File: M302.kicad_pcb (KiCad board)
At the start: 2 copper layers, 68.6 x 53.3 mm, 22 parts, among them J1 I2C-SHT3x, J2 I2C-ThmCp, J3 I2C-3, J4 I2C-4, J5 I2C-D400, J6 W5500, J7 IM920, J8 PWR, P1 Power, P2 Analog, P3 Digital, P4 Digital, P5 CONN_01X01, P6 CONN_01X01, P7 CONN_01X01, P8 CONN_01X01, SW1 CPU, SW2 D400, SW3 IM920, U1 SFE-BOB-12009

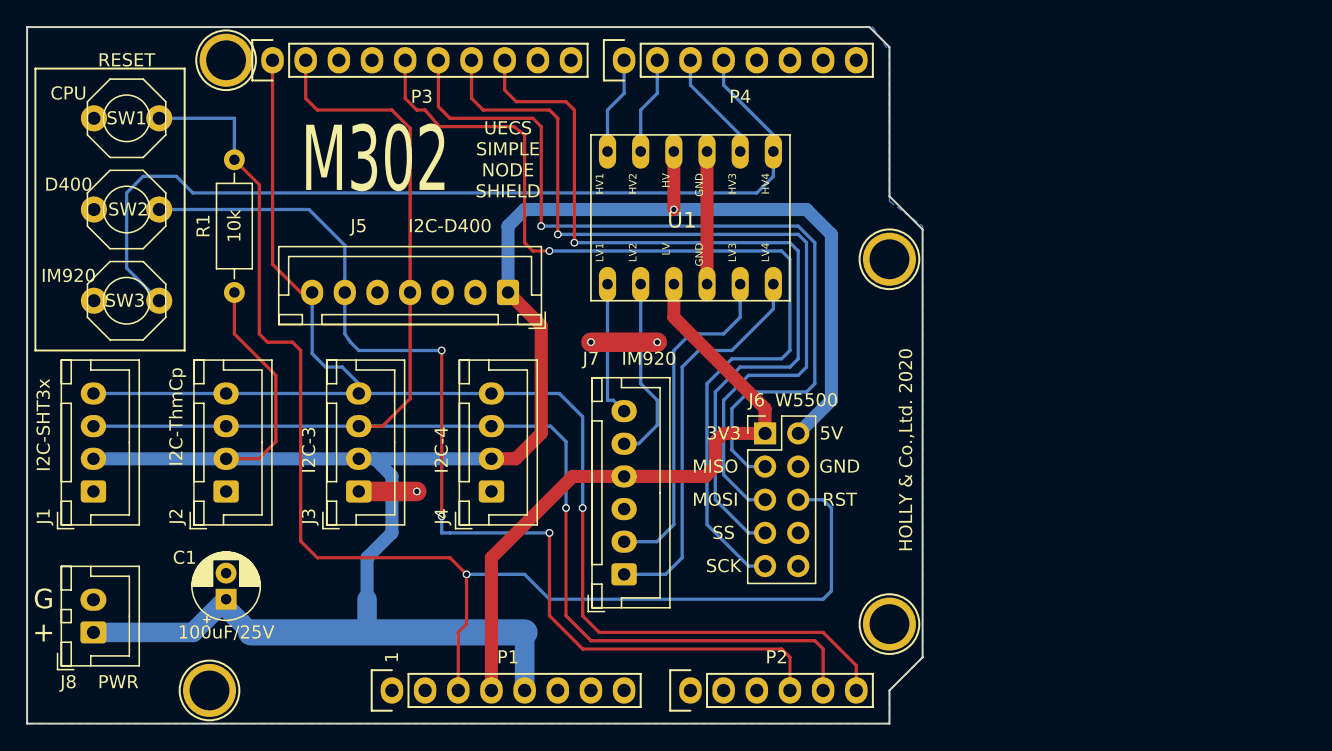
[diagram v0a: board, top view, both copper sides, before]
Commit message: sch: 1.10 PullUp抵抗とアナログインプットを増やす
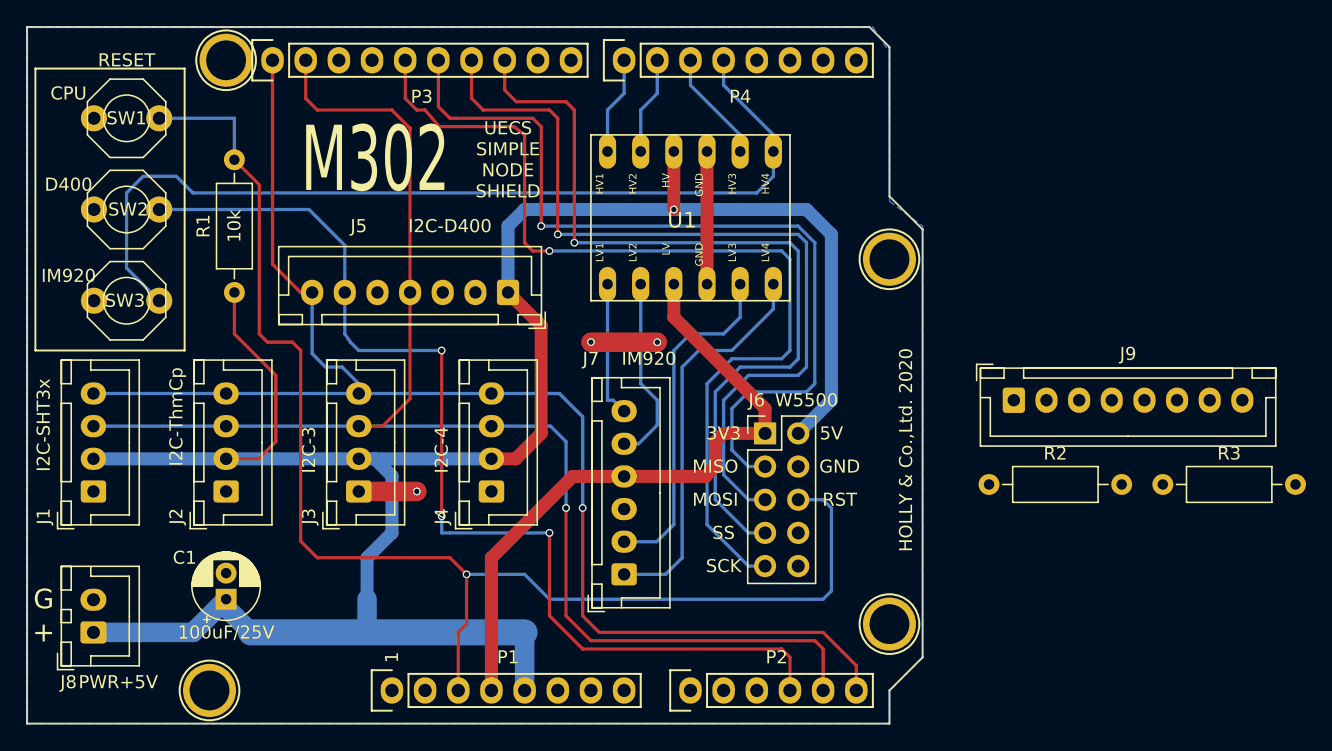
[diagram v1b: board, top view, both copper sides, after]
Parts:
- added J9: ANALOG-IN, Connector_JST:JST_XH_B8B-XH-A_1x08_P2.50mm_Vertical, F.Cu at (186.6, 101.6)
- added R2: 10k, Resistor_THT:R_Axial_DIN0207_L6.3mm_D2.5mm_P10.16mm_Horizontal, F.Cu at (184.7, 108.0)
- added R3: 10k, Resistor_THT:R_Axial_DIN0207_L6.3mm_D2.5mm_P10.16mm_Horizontal, F.Cu at (198.0, 108.0)
- J8: value PWR -> PWR+5V
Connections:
- J5 pad 6: /A3 -> /3(**)
- P2 pad 1: /A0 -> Net-(J9-Pad1)
- P2 pad 2: /A1 -> Net-(J9-Pad3)
- P2 pad 3: /A2 -> Net-(J9-Pad5)
- P2 pad 4: /A3 -> Net-(J9-Pad7)
- SW2 pad 2: /A3 -> /3(**)

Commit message: M302改 v1.10 PCB作業途中
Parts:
- R1, R2, R3: footprint Resistor_THT:R_Axial_DIN0207_L6.3mm_D2.5mm_P10.16mm_Horizontal -> Resistor_THT:R_Axial_DIN0207_L6.3mm_D2.5mm_P7.62mm_Horizontal
- moved R2 60.1 mm to (127.5, 89.5), turned to 90 degrees
- moved J9 40.7 mm to (149.1, 117.5), turned to 90 degrees
- moved R3 38.3 mm to (172.6, 79.4), turned to 270 degrees
- moved J4 5.72 mm to (140.8, 108.6)
- moved R1 4.45 mm to (124.6, 89.5)
- moved J3 3.81 mm to (132.6, 108.6)
- moved J2 1.91 mm to (124.3, 108.6)
- moved J7 1.27 mm to (158.0, 114.9)
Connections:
- P2 pad 5: /A4(SDA) -> Net-(P2-Pad5)
- P2 pad 6: /A5(SCL) -> Net-(P2-Pad6)
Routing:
- net /A3: track 81.0 -> 0.00 mm, vias 3 -> 0
- net /A5(SCL): track 107.4 -> 60.0 mm, vias 1 -> 0
- net /A4(SDA): track 111.3 -> 67.9 mm, vias 1 -> 0
- net +3V3: track 50.5 -> 14.3 mm
- net /3(**): track 0.00 -> 18.6 mm
- net +5V: track 171.7 -> 160.0 mm
- net /Reset: track 102.4 -> 90.8 mm
- net (no net): track 5.08 -> 0.00 mm, vias 2 -> 0
- net GND: track 14.6 -> 10.2 mm

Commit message: pcb: M302改 v1.10 PCB作業一旦終了
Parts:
- moved J9 1.27 mm to (150.4, 117.5)
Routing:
- net +3V3: track 14.3 -> 73.6 mm
- net /3(**): track 18.6 -> 67.5 mm, vias 0 -> 2
- net /Reset: track 90.8 -> 133.9 mm, vias 1 -> 2
- net Net-(J9-Pad7): track 0.00 -> 36.1 mm
- net Net-(J9-Pad5): track 0.00 -> 29.1 mm
- net Net-(J9-Pad3): track 0.00 -> 22.3 mm
- net +5V: track 160.0 -> 176.9 mm, vias 1 -> 2
- net Net-(J9-Pad1): track 0.00 -> 15.0 mm
- net GND: track 10.2 -> 24.1 mm, vias 1 -> 61
- net /A4(SDA): track 67.9 -> 58.4 mm, vias 0 -> 1
- net /4: track 70.9 -> 77.5 mm
- net /A5(SCL): track 60.0 -> 54.3 mm
- net Net-(J7-Pad2): track 26.4 -> 25.1 mm
- net Net-(J7-Pad1): track 30.3 -> 29.0 mm
- net /13(SCK): track 73.3 -> 74.4 mm
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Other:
- board text added: "HOLLY & Co.,Ltd. 2021"
- board text added: "K A I"
- board text removed: "HOLLY & Co.,Ltd. 2020"

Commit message: sche: board: docs:
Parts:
- added C2: 0.01μF, Capacitor_THT:C_Disc_D3.0mm_W2.0mm_P2.50mm, F.Cu at (138.3, 119.4)
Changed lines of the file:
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@@
-(kicad_pcb (version 20171130) (host pcbnew 5.1.5+dfsg1-2build2)
+(kicad_pcb (version 20171130) (host pcbnew 5.1.6-c6e7f7d~87~ubuntu18.04.1)
   (general
     (thickness 1.6)
@@
     (tracks 322)
     (zones 0)
-    (modules 25)
+    (modules 26)
     (nets 43)
   )
@@
     (add_net "Net-(P8-Pad1)")
   )
+  (module Capacitor_THT:C_Disc_D3.0mm_W2.0mm_P2.50mm (layer F.Cu)
+    (at 138.303 119.38 90)
+    (descr "C, Disc series, Radial, pin pitch=2.50mm, , diameter*width=3*2mm^2, Capacitor")
+    (tags "C Disc series Radial pin pitch 2.50mm  diameter 3mm width 2mm Capacitor")
+    (fp_text reference C2 (at 3.175 -2.54 180) (layer F.SilkS)
+      (effects (font (size 1 1) (thickness 0.15)))
+    )
+    (fp_text value 0.01μF (at 0.635 4.445 180) (layer F.SilkS)
+      (effects (font (size 1 1) (thickness 0.15)))
+    )
+    (fp_line (start 3.55 -1.25) (end -1.05 -1.25) (layer F.CrtYd) (width 0.05))
+    (fp_line (start 3.55 1.25) (end 3.55 -1.25) (layer F.CrtYd) (width 0.05))
+    (fp_line (start -1.05 1.25) (end 3.55 1.25) (layer F.CrtYd) (width 0.05))
+    (fp_line (start -1.05 -1.25) (end -1.05 1.25) (layer F.CrtYd) (width 0.05))
+    (fp_line (start 2.87 1.055) (end 2.87 1.12) (layer F.SilkS) (width 0.12))
+    (fp_line (start 2.87 -1.12) (end 2.87 -1.055) (layer F.SilkS) (width 0.12))
+    (fp_line (start -0.37 1.055) (end -0.37 1.12) (layer F.SilkS) (width 0.12))
+    (fp_line (start -0.37 -1.12) (end -0.37 -1.055) (layer F.SilkS) (width 0.12))
+    (fp_line (start -0.37 1.12) (end 2.87 1.12) (layer F.SilkS) (width 0.12))
+    (fp_line (start -0.37 -1.12) (end 2.87 -1.12) (layer F.SilkS) (width 0.12))
+    (fp_line (start 2.75 -1) (end -0.25 -1) (layer F.Fab) (width 0.1))
+    (fp_line (start 2.75 1) (end 2.75 -1) (layer F.Fab) (width 0.1))
+    (fp_line (start -0.25 1) (end 2.75 1) (layer F.Fab) (width 0.1))
+    (fp_line (start -0.25 -1) (end -0.25 1) (layer F.Fab) (width 0.1))
+    (fp_text user %R (at 1.25 0 90) (layer F.Fab)
+      (effects (font (size 0.6 0.6) (thickness 0.09)))
+    )
+    (pad 2 thru_hole circle (at 2.5 0 90) (size 1.6 1.6) (drill 0.8) (layers *.Cu *.Mask)
+      (net 4 GND))
+    (pad 1 thru_hole circle (at 0 0 90) (size 1.6 1.6) (drill 0.8) (layers *.Cu *.Mask)
+      (net 3 +5V))
+    (model ${KISYS3DMOD}/Capacitor_THT.3dshapes/C_Disc_D3.0mm_W2.0mm_P2.50mm.wrl
+      (at (xyz 0 0 0))
+      (scale (xyz 1 1 1))
+      (rotate (xyz 0 0 0))
+    )
+  )
   (module Connector_JST:JST_XH_B8B-XH-A_1x08_P2.50mm_Vertical (layer F.Cu)
     (at 150.368 117.475 90)
@@
       (effects (font (size 1 1) (thickness 0.15)))
     )
-    (fp_text user %R (at 3.81 0 90) (layer F.Fab)
-      (effects (font (size 1 1) (thickness 0.15)))
-    )
     (fp_line (start 0.66 -1.25) (end 0.66 1.25) (layer F.Fab) (width 0.1))
     (fp_line (start 0.66 1.25) (end 6.96 1.25) (layer F.Fab) (width 0.1))
@@
     (fp_line (start 8.67 1.5) (end 8.67 -1.5) (layer F.CrtYd) (width 0.05))
     (fp_line (start 8.67 -1.5) (end -1.05 -1.5) (layer F.CrtYd) (width 0.05))
+    (fp_text user %R (at 3.81 0 90) (layer F.Fab)
+      (effects (font (size 1 1) (thickness 0.15)))
+    )
     (pad 2 thru_hole oval (at 7.62 0 270) (size 1.6 1.6) (drill 0.8) (layers *.Cu *.Mask)
       (net 3 +5V))
@@
     )
     (fp_text value 10k (at -3.091349 -0.049447 90) (layer F.Fab)
-      (effects (font (size 1 1) (thickness 0.15)))
-    )
-    (fp_text user %R (at 10.16 0 90) (layer F.Fab)
       (effects (font (size 1 1) (thickness 0.15)))
     )
@@
     (fp_line (start 8.67 1.5) (end 8.67 -1.5) (layer F.CrtYd) (width 0.05))
     (fp_line (start 8.67 -1.5) (end -1.05 -1.5) (layer F.CrtYd) (width 0.05))
+    (fp_text user %R (at 10.16 0 90) (layer F.Fab)
+      (effects (font (size 1 1) (thickness 0.15)))
+    )
     (pad 2 thru_hole oval (at 7.62 0 90) (size 1.6 1.6) (drill 0.8) (layers *.Cu *.Mask)
       (net 14 "/3(**)"))
@@
     )
     (fp_text value 10k (at -3.175 -0.238835 90) (layer F.Fab)
-      (effects (font (size 1 1) (thickness 0.15)))
-    )
-    (fp_text user %R (at 10.16 0 90) (layer F.Fab)
       (effects (font (size 1 1) (thickness 0.15)))
     )
@@
     (fp_line (start 8.67 1.5) (end 8.67 -1.5) (layer F.CrtYd) (width 0.05))
     (fp_line (start 8.67 -1.5) (end -1.05 -1.5) (layer F.CrtYd) (width 0.05))
+    (fp_text user %R (at 10.16 0 90) (layer F.Fab)
+      (effects (font (size 1 1) (thickness 0.15)))
+    )
     (pad 2 thru_hole oval (at 7.62 0 90) (size 1.6 1.6) (drill 0.8) (layers *.Cu *.Mask)
       (net 2 /Reset))
@@
   (gr_line (start 120.523 82.55) (end 120.523 93.98) (angle 90) (layer Dwgs.User) (width 0.15))
   (gr_line (start 104.648 82.55) (end 120.523 82.55) (angle 90) (layer Dwgs.User) (width 0.15))
-  (segment (start 133.223 116.205) (end 133.223 116.205) (width 3) (layer F.Cu) (net 4))
-  (segment (start 129.413 97.155) (end 129.413 97.155) (width 0.25) (layer F.Cu) (net 4))
-  (segment (start 129.413 97.155) (end 135.763 97.155) (width 3) (layer F.Cu) (net 4))
-  (via (at 129.413 97.155) (size 0.6) (drill 0.4) (layers F.Cu B.Cu) (net 4))
-  (segment (start 135.763 97.155) (end 135.763 97.155) (width 0.25) (layer F.Cu) (net 4))
-  (via (at 135.763 97.155) (size 0.6) (drill 0.4) (layers F.Cu B.Cu) (net 4))
   (segment (start 142.748 118.745) (end 142.748 114.935) (width 0.25) (layer F.Cu) (net 2))
   (segment (start 122.666835 80.01) (end 124.571835 81.915) (width 0.25) (layer B.Cu) (net 2))
@@
   (segment (start 124.333 106.085) (end 136.398 106.085) (width 2) (layer B.Cu) (net 3))
   (segment (start 116.078 106.085) (end 124.333 106.085) (width 2) (layer B.Cu) (net 3))
+  (segment (start 133.223 116.205) (end 133.223 116.205) (width 3) (layer F.Cu) (net 4))
+  (segment (start 129.413 97.155) (end 129.413 97.155) (width 0.25) (layer F.Cu) (net 4))
+  (segment (start 129.413 97.155) (end 135.763 97.155) (width 3) (layer F.Cu) (net 4))
+  (via (at 129.413 97.155) (size 0.6) (drill 0.4) (layers F.Cu B.Cu) (net 4))
+  (segment (start 135.763 97.155) (end 135.763 97.155) (width 0.25) (layer F.Cu) (net 4))
+  (via (at 135.763 97.155) (size 0.6) (drill 0.4) (layers F.Cu B.Cu) (net 4))
   (segment (start 163.068 82.55) (end 163.068 92.71) (width 1) (layer F.Cu) (net 4))
   (via (at 140.843 108.585) (size 0.6) (drill 0.4) (layers F.Cu B.Cu) (net 4))

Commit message: rel: 1.10
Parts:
- moved R2 0.64 mm to (128.1, 89.5)
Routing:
- net GND: vias 61 -> 47
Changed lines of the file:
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@@
     (thickness 1.6)
     (drawings 56)
-    (tracks 322)
+    (tracks 307)
     (zones 0)
     (modules 26)
@@
       (drillshape 0)
       (scaleselection 1)
-      (outputdirectory "CAMOUT2/"))
+      (outputdirectory "CAMOUT-1.10"))
   )
   (net 0 "")
@@
   )
   (module Resistor_THT:R_Axial_DIN0207_L6.3mm_D2.5mm_P7.62mm_Horizontal (layer F.Cu)
-    (at 127.508 89.535 90)
+    (at 128.143 89.535 90)
     (descr "Resistor, Axial_DIN0207 series, Axial, Horizontal, pin pitch=7.62mm, 0.25W = 1/4W, length*diameter=6.3*2.5mm^2, http://cdn-reichelt.de/documents/datenblatt/B400/1_4W%23YAG.pdf")
     (tags "Resistor Axial_DIN0207 series Axial Horizontal pin pitch 7.62mm 0.25W = 1/4W length 6.3mm diameter 2.5mm")
@@
   (via (at 129.413 97.155) (size 0.6) (drill 0.4) (layers F.Cu B.Cu) (net 4))
   (segment (start 135.763 97.155) (end 135.763 97.155) (width 0.25) (layer F.Cu) (net 4))
-  (via (at 135.763 97.155) (size 0.6) (drill 0.4) (layers F.Cu B.Cu) (net 4))
   (segment (start 163.068 82.55) (end 163.068 92.71) (width 1) (layer F.Cu) (net 4))
   (via (at 140.843 108.585) (size 0.6) (drill 0.4) (layers F.Cu B.Cu) (net 4))
-  (via (at 130.048 97.155) (size 0.6) (drill 0.4) (layers F.Cu B.Cu) (net 4))
   (via (at 130.683 97.155) (size 0.6) (drill 0.4) (layers F.Cu B.Cu) (net 4))
   (via (at 135.128 97.155) (size 0.6) (drill 0.4) (layers F.Cu B.Cu) (net 4))
-  (via (at 134.493 97.155) (size 0.6) (drill 0.4) (layers F.Cu B.Cu) (net 4))
-  (via (at 131.318 97.155) (size 0.6) (drill 0.4) (layers F.Cu B.Cu) (net 4))
   (segment (start 133.223 114.935) (end 133.223 120.65) (width 3.5) (layer F.Cu) (net 4))
   (via (at 133.223 116.205) (size 0.6) (drill 0.4) (layers F.Cu B.Cu) (net 4))
@@
   (via (at 131.953 114.935) (size 0.6) (drill 0.4) (layers F.Cu B.Cu) (net 4))
   (via (at 133.223 113.665) (size 0.6) (drill 0.4) (layers F.Cu B.Cu) (net 4))
-  (via (at 128.778 97.155) (size 0.6) (drill 0.4) (layers F.Cu B.Cu) (net 4))
-  (via (at 129.413 96.52) (size 0.6) (drill 0.4) (layers F.Cu B.Cu) (net 4))
   (via (at 130.048 96.52) (size 0.6) (drill 0.4) (layers F.Cu B.Cu) (net 4))
-  (via (at 130.683 96.52) (size 0.6) (drill 0.4) (layers F.Cu B.Cu) (net 4))
   (via (at 131.318 96.52) (size 0.6) (drill 0.4) (layers F.Cu B.Cu) (net 4))
   (via (at 131.318 97.79) (size 0.6) (drill 0.4) (layers F.Cu B.Cu) (net 4))
-  (via (at 130.683 97.79) (size 0.6) (drill 0.4) (layers F.Cu B.Cu) (net 4))
   (via (at 130.048 97.79) (size 0.6) (drill 0.4) (layers F.Cu B.Cu) (net 4))
-  (via (at 129.413 97.79) (size 0.6) (drill 0.4) (layers F.Cu B.Cu) (net 4))
-  (via (at 133.858 96.52) (size 0.6) (drill 0.4) (layers F.Cu B.Cu) (net 4))
   (via (at 134.493 97.79) (size 0.6) (drill 0.4) (layers F.Cu B.Cu) (net 4))
   (via (at 134.493 96.52) (size 0.6) (drill 0.4) (layers F.Cu B.Cu) (net 4))
-  (via (at 135.128 96.52) (size 0.6) (drill 0.4) (layers F.Cu B.Cu) (net 4))
-  (via (at 135.763 96.52) (size 0.6) (drill 0.4) (layers F.Cu B.Cu) (net 4))
   (via (at 136.398 97.155) (size 0.6) (drill 0.4) (layers F.Cu B.Cu) (net 4))
   (via (at 135.763 97.79) (size 0.6) (drill 0.4) (layers F.Cu B.Cu) (net 4))
-  (via (at 135.128 97.79) (size 0.6) (drill 0.4) (layers F.Cu B.Cu) (net 4))
   (via (at 133.858 97.155) (size 0.6) (drill 0.4) (layers F.Cu B.Cu) (net 4))
   (via (at 128.778 96.52) (size 0.6) (drill 0.4) (layers F.Cu B.Cu) (net 4))
   (via (at 128.778 97.79) (size 0.6) (drill 0.4) (layers F.Cu B.Cu) (net 4))
-  (via (at 136.398 97.79) (size 0.6) (drill 0.4) (layers F.Cu B.Cu) (net 4))
-  (via (at 136.398 96.52) (size 0.6) (drill 0.4) (layers F.Cu B.Cu) (net 4))
+  (via (at 135.763 96.52) (size 0.6) (drill 0.4) (layers F.Cu B.Cu) (net 4))
   (segment (start 136.398 103.585) (end 140.843 103.585) (width 0.25) (layer B.Cu) (net 6))
   (segment (start 116.078 103.585) (end 136.398 103.585) (width 0.25) (layer B.Cu) (net 6))
@@
   (segment (start 132.588 86.995) (end 135.1416 89.5486) (width 0.25) (layer B.Cu) (net 14))
   (segment (start 121.118 86.995) (end 132.588 86.995) (width 0.25) (layer B.Cu) (net 14))
-  (segment (start 127.508 81.915) (end 127.508 86.995) (width 0.25) (layer F.Cu) (net 14))
-  (segment (start 127.508 86.995) (end 127.508 86.995) (width 0.25) (layer F.Cu) (net 14))
-  (via (at 127.508 86.995) (size 0.6) (drill 0.4) (layers F.Cu B.Cu) (net 14))
-  (segment (start 127.508 80.78363) (end 128.28163 80.01) (width 0.25) (layer B.Cu) (net 14))
-  (segment (start 127.508 81.915) (end 127.508 80.78363) (width 0.25) (layer B.Cu) (net 14))
-  (segment (start 128.28163 80.01) (end 153.543 80.01) (width 0.25) (layer B.Cu) (net 14))
   (segment (start 153.543 80.01) (end 153.543 80.01) (width 0.25) (layer B.Cu) (net 14))
   (via (at 153.543 80.01) (size 0.6) (drill 0.4) (layers F.Cu B.Cu) (net 14))
@@
   (segment (start 166.878 77.47) (end 166.878 75.565) (width 0.25) (layer F.Cu) (net 14))
   (segment (start 164.338 80.01) (end 166.878 77.47) (width 0.25) (layer F.Cu) (net 14))
+  (segment (start 128.143 80.714315) (end 128.28163 80.01) (width 0.25) (layer B.Cu) (net 14))
+  (segment (start 128.28163 80.01) (end 153.543 80.01) (width 0.25) (layer B.Cu) (net 14))
+  (segment (start 128.143 81.915) (end 128.143 80.714315) (width 0.25) (layer B.Cu) (net 14))
+  (segment (start 128.143 81.915) (end 128.143 86.995) (width 0.25) (layer F.Cu) (net 14))
+  (via (at 128.143 86.995) (size 0.6) (drill 0.4) (layers F.Cu B.Cu) (net 14))
   (segment (start 166.243 114.3) (end 167.513 114.3) (width 0.25) (layer B.Cu) (net 22))
   (segment (start 168.783 98.425) (end 164.973 98.425) (width 0.25) (layer B.Cu) (net 22))
